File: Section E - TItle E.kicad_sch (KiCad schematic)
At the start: 0 parts

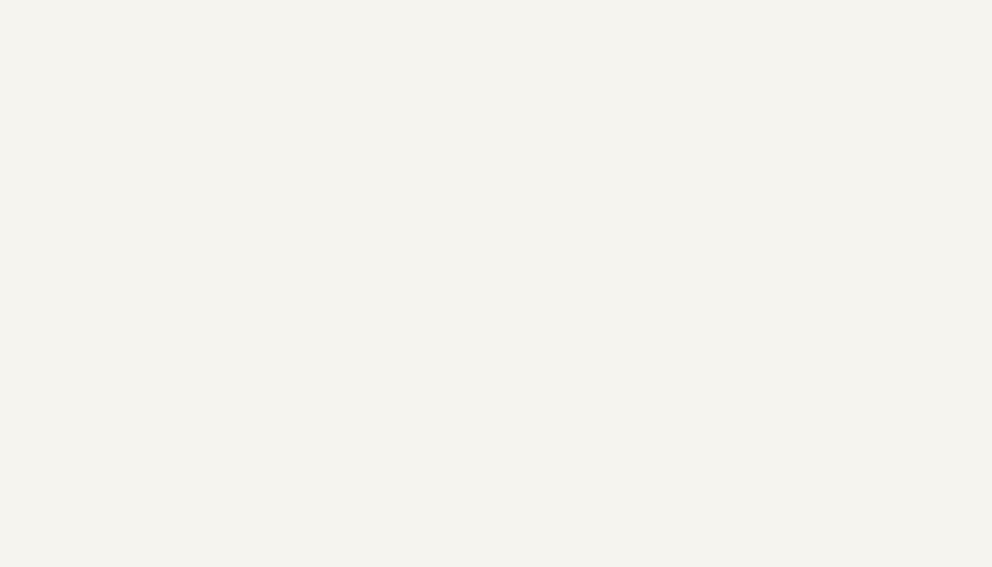
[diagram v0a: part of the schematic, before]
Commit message: [ADD TPS6108]
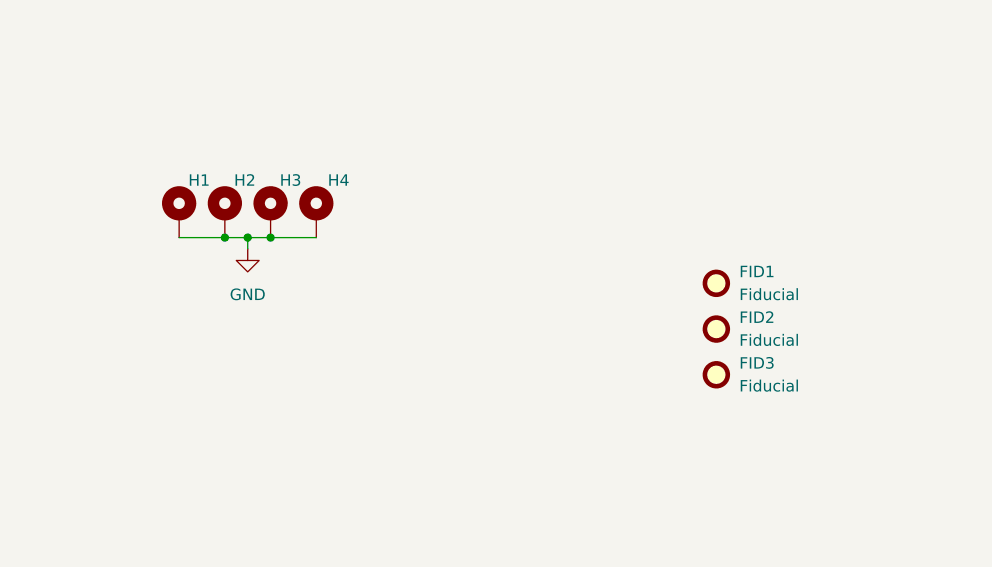
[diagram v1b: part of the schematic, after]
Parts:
- added FID1, FID2, FID3: Fiducial, Fiducial:Fiducial_1.5mm_Mask3mm, symbol Mechanical:Fiducial
- added H1, H2, H3, H4: MountingHole_Pad, MountingHole:MountingHole_3.2mm_M3_Pad_Via, symbol Mechanical:MountingHole_Pad
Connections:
- new net GND: H1.1, H2.1, H3.1, H4.1
